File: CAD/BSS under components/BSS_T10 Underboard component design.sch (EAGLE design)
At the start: 9 parts, among them IC1 7805DT

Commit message: Board labels
Improved labeling of board
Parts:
- TO_SEN, VOLT_IN: value (none) -> MA03-1
- renumbered CBP1 to C3, LED1 to LED
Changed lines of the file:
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@@
 <grid distance="0.1" unitdist="inch" unit="inch" style="lines" multiple="1" display="no" altdistance="0.01" altunitdist="inch" altunit="inch"/>
 <layers>
-<layer number="1" name="Top" color="4" fill="1" visible="no" active="no"/>
-<layer number="16" name="Bottom" color="1" fill="1" visible="no" active="no"/>
-<layer number="17" name="Pads" color="2" fill="1" visible="no" active="no"/>
-<layer number="18" name="Vias" color="2" fill="1" visible="no" active="no"/>
-<layer number="19" name="Unrouted" color="6" fill="1" visible="no" active="no"/>
-<layer number="20" name="Dimension" color="15" fill="1" visible="no" active="no"/>
-<layer number="21" name="tPlace" color="7" fill="1" visible="no" active="no"/>
-<layer number="22" name="bPlace" color="7" fill="1" visible="no" active="no"/>
-<layer number="23" name="tOrigins" color="15" fill="1" visible="no" active="no"/>
-<layer number="24" name="bOrigins" color="15" fill="1" visible="no" active="no"/>
-<layer number="25" name="tNames" color="7" fill="1" visible="no" active="no"/>
-<layer number="26" name="bNames" color="7" fill="1" visible="no" active="no"/>
-<layer number="27" name="tValues" color="7" fill="1" visible="no" active="no"/>
-<layer number="28" name="bValues" color="7" fill="1" visible="no" active="no"/>
+<layer number="1" name="Top" color="4" fill="1" visible="yes" active="no"/>
+<layer number="16" name="Bottom" color="1" fill="1" visible="yes" active="no"/>
+<layer number="17" name="Pads" color="2" fill="1" visible="yes" active="no"/>
+<layer number="18" name="Vias" color="2" fill="1" visible="yes" active="no"/>
+<layer number="19" name="Unrouted" color="6" fill="1" visible="yes" active="no"/>
+<layer number="20" name="Dimension" color="15" fill="1" visible="yes" active="no"/>
+<layer number="21" name="tPlace" color="7" fill="1" visible="yes" active="no"/>
+<layer number="22" name="bPlace" color="7" fill="1" visible="yes" active="no"/>
+<layer number="23" name="tOrigins" color="15" fill="1" visible="yes" active="no"/>
+<layer number="24" name="bOrigins" color="15" fill="1" visible="yes" active="no"/>
+<layer number="25" name="tNames" color="7" fill="1" visible="yes" active="no"/>
+<layer number="26" name="bNames" color="7" fill="1" visible="yes" active="no"/>
+<layer number="27" name="tValues" color="7" fill="1" visible="yes" active="no"/>
+<layer number="28" name="bValues" color="7" fill="1" visible="yes" active="no"/>
 <layer number="29" name="tStop" color="7" fill="3" visible="no" active="no"/>
 <layer number="30" name="bStop" color="7" fill="6" visible="no" active="no"/>
@@
 <layer number="35" name="tGlue" color="7" fill="4" visible="no" active="no"/>
 <layer number="36" name="bGlue" color="7" fill="5" visible="no" active="no"/>
-<layer number="37" name="tTest" color="7" fill="1" visible="no" active="no"/>
-<layer number="38" name="bTest" color="7" fill="1" visible="no" active="no"/>
+<layer number="37" name="tTest" color="7" fill="1" visible="yes" active="no"/>
+<layer number="38" name="bTest" color="7" fill="1" visible="yes" active="no"/>
 <layer number="39" name="tKeepout" color="4" fill="11" visible="no" active="no"/>
 <layer number="40" name="bKeepout" color="1" fill="11" visible="no" active="no"/>
@@
 <layer number="44" name="Drills" color="7" fill="1" visible="no" active="no"/>
 <layer number="45" name="Holes" color="7" fill="1" visible="no" active="no"/>
-<layer number="46" name="Milling" color="3" fill="1" visible="no" active="no"/>
-<layer number="47" name="Measures" color="7" fill="1" visible="no" active="no"/>
-<layer number="48" name="Document" color="7" fill="1" visible="no" active="no"/>
-<layer number="49" name="Reference" color="7" fill="1" visible="no" active="no"/>
-<layer number="51" name="tDocu" color="7" fill="1" visible="no" active="no"/>
-<layer number="52" name="bDocu" color="7" fill="1" visible="no" active="no"/>
+<layer number="46" name="Milling" color="3" fill="1" visible="yes" active="no"/>
+<layer number="47" name="Measures" color="7" fill="1" visible="yes" active="no"/>
+<layer number="48" name="Document" color="7" fill="1" visible="yes" active="no"/>
+<layer number="49" name="Reference" color="7" fill="1" visible="yes" active="no"/>
+<layer number="51" name="tDocu" color="7" fill="1" visible="yes" active="no"/>
+<layer number="52" name="bDocu" color="7" fill="1" visible="yes" active="no"/>
 <layer number="91" name="Nets" color="2" fill="1" visible="yes" active="yes"/>
 <layer number="92" name="Busses" color="1" fill="1" visible="yes" active="yes"/>
@@
 <part name="P+2" library="supply1" deviceset="+5V" device=""/>
 <part name="GND1" library="supply1" deviceset="GND" device=""/>
-<part name="CBP1" library="rcl" deviceset="C-EU" device="C0805" value=".1uF"/>
+<part name="C3" library="rcl" deviceset="C-EU" device="C0805" value=".1uF"/>
 <part name="C1" library="rcl" deviceset="C-EU" device="C0805" value=".1uF"/>
 <part name="C2" library="rcl" deviceset="C-EU" device="C0805" value=".1uF"/>
@@
 <part name="R1" library="rcl" deviceset="R-US_" device="R0805" value="1k"/>
 <part name="GND6" library="supply1" deviceset="GND" device=""/>
-<part name="LED1" library="led" deviceset="LED" device="5MM"/>
+<part name="LED" library="led" deviceset="LED" device="5MM"/>
 <part name="VOLT_IN" library="con-lstb" deviceset="MA03-1" device=""/>
 <part name="TO_SEN" library="con-lstb" deviceset="MA03-1" device=""/>
@@
 <instance part="P+2" gate="1" x="38.1" y="53.34"/>
 <instance part="GND1" gate="1" x="38.1" y="5.08"/>
-<instance part="CBP1" gate="G$1" x="-22.86" y="27.94"/>
+<instance part="C3" gate="G$1" x="-22.86" y="27.94"/>
 <instance part="C1" gate="G$1" x="93.98" y="73.66"/>
 <instance part="C2" gate="G$1" x="55.88" y="73.66"/>
@@
 <instance part="R1" gate="G$1" x="48.26" y="7.62" rot="R90"/>
 <instance part="GND6" gate="1" x="48.26" y="-2.54"/>
-<instance part="LED1" gate="G$1" x="48.26" y="20.32"/>
+<instance part="LED" gate="G$1" x="48.26" y="20.32"/>
 <instance part="VOLT_IN" gate="G$1" x="30.48" y="76.2"/>
 <instance part="TO_SEN" gate="G$1" x="106.68" y="25.4" rot="MR0"/>
@@
 <pinref part="P+2" gate="1" pin="+5V"/>
 <wire x1="38.1" y1="38.1" x2="38.1" y2="45.72" width="0.1524" layer="91"/>
-<pinref part="CBP1" gate="G$1" pin="1"/>
+<pinref part="C3" gate="G$1" pin="1"/>
 <wire x1="38.1" y1="45.72" x2="38.1" y2="50.8" width="0.1524" layer="91"/>
 <wire x1="38.1" y1="45.72" x2="-22.86" y2="45.72" width="0.1524" layer="91"/>
@@
 <wire x1="38.1" y1="20.32" x2="38.1" y2="10.16" width="0.1524" layer="91"/>
 <pinref part="GND1" gate="1" pin="GND"/>
-<pinref part="CBP1" gate="G$1" pin="2"/>
+<pinref part="C3" gate="G$1" pin="2"/>
 <wire x1="38.1" y1="10.16" x2="38.1" y2="7.62" width="0.1524" layer="91"/>
 <wire x1="-22.86" y1="22.86" x2="-22.86" y2="10.16" width="0.1524" layer="91"/>
@@
 <pinref part="R1" gate="G$1" pin="2"/>
 <wire x1="48.26" y1="15.24" x2="48.26" y2="12.7" width="0.1524" layer="91"/>
-<pinref part="LED1" gate="G$1" pin="C"/>
+<pinref part="LED" gate="G$1" pin="C"/>
 </segment>
 </net>
@@
 <net name="N$4" class="0">
 <segment>
-<pinref part="LED1" gate="G$1" pin="A"/>
+<pinref part="LED" gate="G$1" pin="A"/>
 <wire x1="48.26" y1="22.86" x2="48.26" y2="30.48" width="0.1524" layer="91"/>
 <pinref part="AVR" gate="G$1" pin="PB2/PCINT2/SCK/ADC1/T0"/>

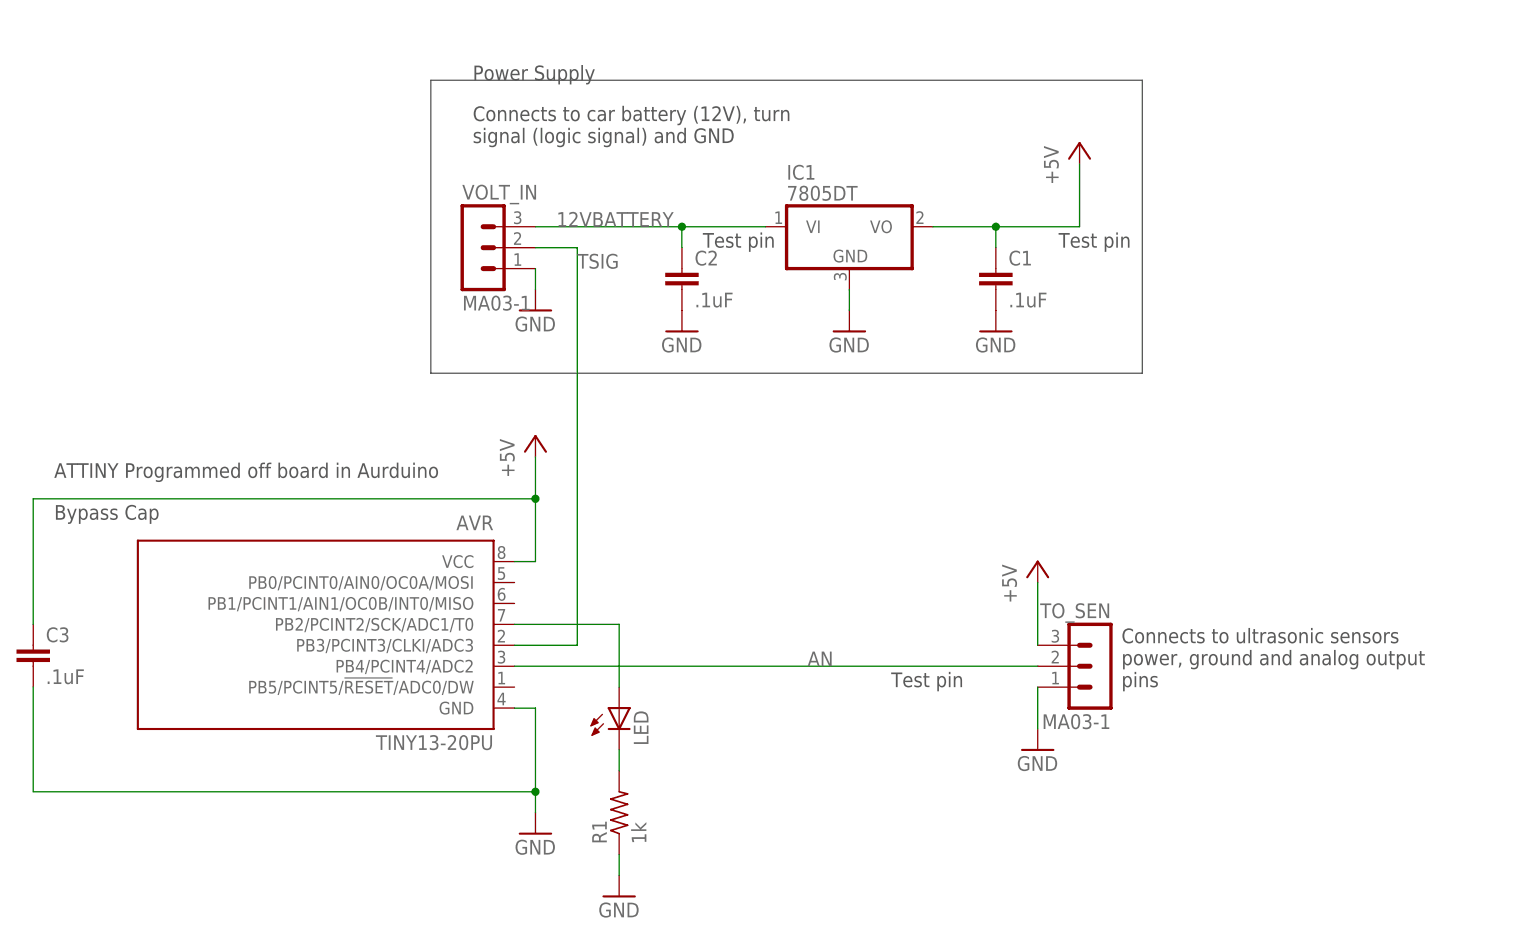
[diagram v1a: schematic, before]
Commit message: Different Pins
Changed pins to AVR
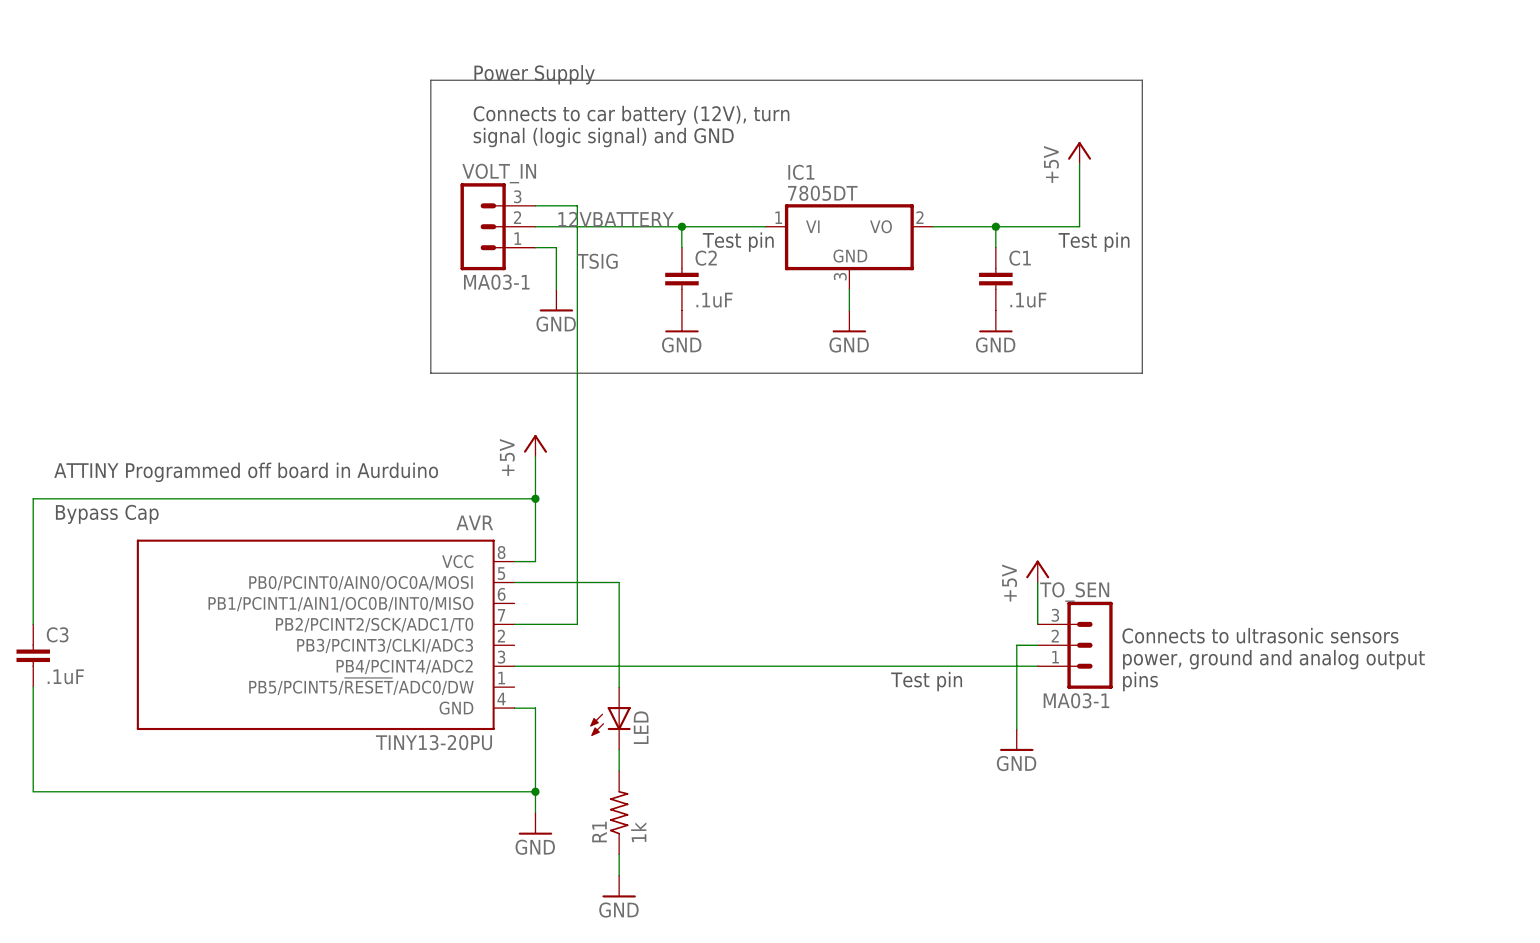
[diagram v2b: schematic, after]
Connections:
- removed net AN: AVR.PB4/PCINT4/ADC2, TO_SEN.2
- new net N$1: AVR.PB4/PCINT4/ADC2, TO_SEN.1
- net 12VBATTERY: now also VOLT_IN.2; no longer VOLT_IN.3
- net GND: now also TO_SEN.2; no longer TO_SEN.1
- net N$4: now also AVR.PB0/PCINT0/AIN0/OC0A/MOSI; no longer AVR.PB2/PCINT2/SCK/ADC1/T0
- net TSIG: now also AVR.PB2/PCINT2/SCK/ADC1/T0, VOLT_IN.3; no longer AVR.PB3/PCINT3/CLKI/ADC3, VOLT_IN.2
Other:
- moved on the sheet: TO_SEN, VOLT_IN
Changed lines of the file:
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@@
 <grid distance="0.1" unitdist="inch" unit="inch" style="lines" multiple="1" display="no" altdistance="0.01" altunitdist="inch" altunit="inch"/>
 <layers>
-<layer number="1" name="Top" color="4" fill="1" visible="yes" active="no"/>
-<layer number="16" name="Bottom" color="1" fill="1" visible="yes" active="no"/>
-<layer number="17" name="Pads" color="2" fill="1" visible="yes" active="no"/>
-<layer number="18" name="Vias" color="2" fill="1" visible="yes" active="no"/>
-<layer number="19" name="Unrouted" color="6" fill="1" visible="yes" active="no"/>
-<layer number="20" name="Dimension" color="15" fill="1" visible="yes" active="no"/>
-<layer number="21" name="tPlace" color="7" fill="1" visible="yes" active="no"/>
-<layer number="22" name="bPlace" color="7" fill="1" visible="yes" active="no"/>
-<layer number="23" name="tOrigins" color="15" fill="1" visible="yes" active="no"/>
-<layer number="24" name="bOrigins" color="15" fill="1" visible="yes" active="no"/>
-<layer number="25" name="tNames" color="7" fill="1" visible="yes" active="no"/>
-<layer number="26" name="bNames" color="7" fill="1" visible="yes" active="no"/>
-<layer number="27" name="tValues" color="7" fill="1" visible="yes" active="no"/>
-<layer number="28" name="bValues" color="7" fill="1" visible="yes" active="no"/>
+<layer number="1" name="Top" color="4" fill="1" visible="no" active="no"/>
+<layer number="16" name="Bottom" color="1" fill="1" visible="no" active="no"/>
+<layer number="17" name="Pads" color="2" fill="1" visible="no" active="no"/>
+<layer number="18" name="Vias" color="2" fill="1" visible="no" active="no"/>
+<layer number="19" name="Unrouted" color="6" fill="1" visible="no" active="no"/>
+<layer number="20" name="Dimension" color="15" fill="1" visible="no" active="no"/>
+<layer number="21" name="tPlace" color="7" fill="1" visible="no" active="no"/>
+<layer number="22" name="bPlace" color="7" fill="1" visible="no" active="no"/>
+<layer number="23" name="tOrigins" color="15" fill="1" visible="no" active="no"/>
+<layer number="24" name="bOrigins" color="15" fill="1" visible="no" active="no"/>
+<layer number="25" name="tNames" color="7" fill="1" visible="no" active="no"/>
+<layer number="26" name="bNames" color="7" fill="1" visible="no" active="no"/>
+<layer number="27" name="tValues" color="7" fill="1" visible="no" active="no"/>
+<layer number="28" name="bValues" color="7" fill="1" visible="no" active="no"/>
 <layer number="29" name="tStop" color="7" fill="3" visible="no" active="no"/>
 <layer number="30" name="bStop" color="7" fill="6" visible="no" active="no"/>
@@
 <layer number="35" name="tGlue" color="7" fill="4" visible="no" active="no"/>
 <layer number="36" name="bGlue" color="7" fill="5" visible="no" active="no"/>
-<layer number="37" name="tTest" color="7" fill="1" visible="yes" active="no"/>
-<layer number="38" name="bTest" color="7" fill="1" visible="yes" active="no"/>
+<layer number="37" name="tTest" color="7" fill="1" visible="no" active="no"/>
+<layer number="38" name="bTest" color="7" fill="1" visible="no" active="no"/>
 <layer number="39" name="tKeepout" color="4" fill="11" visible="no" active="no"/>
 <layer number="40" name="bKeepout" color="1" fill="11" visible="no" active="no"/>
@@
 <layer number="44" name="Drills" color="7" fill="1" visible="no" active="no"/>
 <layer number="45" name="Holes" color="7" fill="1" visible="no" active="no"/>
-<layer number="46" name="Milling" color="3" fill="1" visible="yes" active="no"/>
-<layer number="47" name="Measures" color="7" fill="1" visible="yes" active="no"/>
-<layer number="48" name="Document" color="7" fill="1" visible="yes" active="no"/>
-<layer number="49" name="Reference" color="7" fill="1" visible="yes" active="no"/>
-<layer number="51" name="tDocu" color="7" fill="1" visible="yes" active="no"/>
-<layer number="52" name="bDocu" color="7" fill="1" visible="yes" active="no"/>
+<layer number="46" name="Milling" color="3" fill="1" visible="no" active="no"/>
+<layer number="47" name="Measures" color="7" fill="1" visible="no" active="no"/>
+<layer number="48" name="Document" color="7" fill="1" visible="no" active="no"/>
+<layer number="49" name="Reference" color="7" fill="1" visible="no" active="no"/>
+<layer number="51" name="tDocu" color="7" fill="1" visible="no" active="no"/>
+<layer number="52" name="bDocu" color="7" fill="1" visible="no" active="no"/>
 <layer number="91" name="Nets" color="2" fill="1" visible="yes" active="yes"/>
 <layer number="92" name="Busses" color="1" fill="1" visible="yes" active="yes"/>
@@
 <instance part="GND6" gate="1" x="48.26" y="-2.54"/>
 <instance part="LED" gate="G$1" x="48.26" y="20.32"/>
-<instance part="VOLT_IN" gate="G$1" x="30.48" y="76.2"/>
-<instance part="TO_SEN" gate="G$1" x="106.68" y="25.4" rot="MR0"/>
-<instance part="GND2" gate="1" x="99.06" y="15.24"/>
+<instance part="VOLT_IN" gate="G$1" x="30.48" y="78.74"/>
+<instance part="TO_SEN" gate="G$1" x="106.68" y="27.94" rot="MR0"/>
+<instance part="GND2" gate="1" x="96.52" y="15.24"/>
 <instance part="FRAME2" gate="G$1" x="-33.02" y="-25.4"/>
 <instance part="IC1" gate="A1" x="76.2" y="78.74"/>
 <instance part="P+1" gate="1" x="99.06" y="38.1"/>
-<instance part="GND7" gate="1" x="38.1" y="68.58"/>
+<instance part="GND7" gate="1" x="40.64" y="68.58"/>
 </instances>
 <busses>
@@
 <segment>
 <pinref part="TO_SEN" gate="G$1" pin="3"/>
-<wire x1="99.06" y1="27.94" x2="99.06" y2="35.56" width="0.1524" layer="91"/>
+<wire x1="99.06" y1="30.48" x2="99.06" y2="35.56" width="0.1524" layer="91"/>
 <pinref part="P+1" gate="1" pin="+5V"/>
 </segment>
@@
 </segment>
 <segment>
-<pinref part="TO_SEN" gate="G$1" pin="1"/>
-<wire x1="99.06" y1="22.86" x2="99.06" y2="17.78" width="0.1524" layer="91"/>
 <pinref part="GND2" gate="1" pin="GND"/>
-</segment>
-<segment>
+<wire x1="96.52" y1="17.78" x2="96.52" y2="27.94" width="0.1524" layer="91"/>
+<pinref part="TO_SEN" gate="G$1" pin="2"/>
+<wire x1="96.52" y1="27.94" x2="99.06" y2="27.94" width="0.1524" layer="91"/>
+</segment>
+<segment>
+<pinref part="GND7" gate="1" pin="GND"/>
+<wire x1="40.64" y1="71.12" x2="40.64" y2="76.2" width="0.1524" layer="91"/>
 <pinref part="VOLT_IN" gate="G$1" pin="1"/>
-<wire x1="38.1" y1="73.66" x2="38.1" y2="71.12" width="0.1524" layer="91"/>
-<pinref part="GND7" gate="1" pin="GND"/>
+<wire x1="40.64" y1="76.2" x2="38.1" y2="76.2" width="0.1524" layer="91"/>
 </segment>
 </net>
 <net name="TSIG" class="0">
 <segment>
-<wire x1="43.18" y1="76.2" x2="43.18" y2="27.94" width="0.1524" layer="91"/>
-<pinref part="VOLT_IN" gate="G$1" pin="2"/>
-<wire x1="43.18" y1="76.2" x2="38.1" y2="76.2" width="0.1524" layer="91"/>
+<wire x1="43.18" y1="81.28" x2="43.18" y2="30.48" width="0.1524" layer="91"/>
 <label x="43.18" y="73.66" size="1.778" layer="95"/>
-<pinref part="AVR" gate="G$1" pin="PB3/PCINT3/CLKI/ADC3"/>
-<wire x1="43.18" y1="27.94" x2="35.56" y2="27.94" width="0.1524" layer="91"/>
+<pinref part="AVR" gate="G$1" pin="PB2/PCINT2/SCK/ADC1/T0"/>
+<wire x1="43.18" y1="30.48" x2="35.56" y2="30.48" width="0.1524" layer="91"/>
+<pinref part="VOLT_IN" gate="G$1" pin="3"/>
+<wire x1="43.18" y1="81.28" x2="38.1" y2="81.28" width="0.1524" layer="91"/>
 </segment>
 </net>
@@
 <wire x1="55.88" y1="76.2" x2="55.88" y2="78.74" width="0.1524" layer="91"/>
 <pinref part="IC1" gate="A1" pin="VI"/>
-<pinref part="VOLT_IN" gate="G$1" pin="3"/>
+<label x="40.64" y="78.74" size="1.778" layer="95"/>
+<pinref part="VOLT_IN" gate="G$1" pin="2"/>
 <wire x1="38.1" y1="78.74" x2="55.88" y2="78.74" width="0.1524" layer="91"/>
 <junction x="55.88" y="78.74"/>
-<label x="40.64" y="78.74" size="1.778" layer="95"/>
-</segment>
-</net>
-<net name="AN" class="0">
+</segment>
+</net>
+<net name="N$4" class="0">
+<segment>
+<pinref part="LED" gate="G$1" pin="A"/>
+<wire x1="48.26" y1="22.86" x2="48.26" y2="35.56" width="0.1524" layer="91"/>
+<pinref part="AVR" gate="G$1" pin="PB0/PCINT0/AIN0/OC0A/MOSI"/>
+<wire x1="48.26" y1="35.56" x2="35.56" y2="35.56" width="0.1524" layer="91"/>
+</segment>
+</net>
+<net name="N$1" class="0">
 <segment>
 <pinref part="AVR" gate="G$1" pin="PB4/PCINT4/ADC2"/>
-<pinref part="TO_SEN" gate="G$1" pin="2"/>
-<wire x1="35.56" y1="25.4" x2="99.06" y2="25.4" width="0.1524" layer="91"/>
-<label x="71.12" y="25.4" size="1.778" layer="95"/>
-</segment>
-</net>
-<net name="N$4" class="0">
-<segment>
-<pinref part="LED" gate="G$1" pin="A"/>
-<wire x1="48.26" y1="22.86" x2="48.26" y2="30.48" width="0.1524" layer="91"/>
-<pinref part="AVR" gate="G$1" pin="PB2/PCINT2/SCK/ADC1/T0"/>
-<wire x1="48.26" y1="30.48" x2="35.56" y2="30.48" width="0.1524" layer="91"/>
-</segment>
-</net>
+<pinref part="TO_SEN" gate="G$1" pin="1"/>
+<wire x1="99.06" y1="25.4" x2="35.56" y2="25.4" width="0.1524" layer="91"/>
+</segment>
+</net>
